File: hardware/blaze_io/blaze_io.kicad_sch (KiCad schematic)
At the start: 58 parts, among them J1 Conn_01x04, J2 Conn_01x04, J3 JTAG, J4 Conn_01x03_Pin, J5 Conn_01x03_Pin, J6 Conn_01x03_Pin, J7 Conn_01x03_Pin, J8 Conn_01x30_Pin, J9 Conn_01x30_Socket, Q1 AO4892, Q2 AO4892, SW1 SW_SPST, SW2 SW_SPDT, U1 4081, U2 TCAN1044VDDFR, U3 STM32H503KBUx

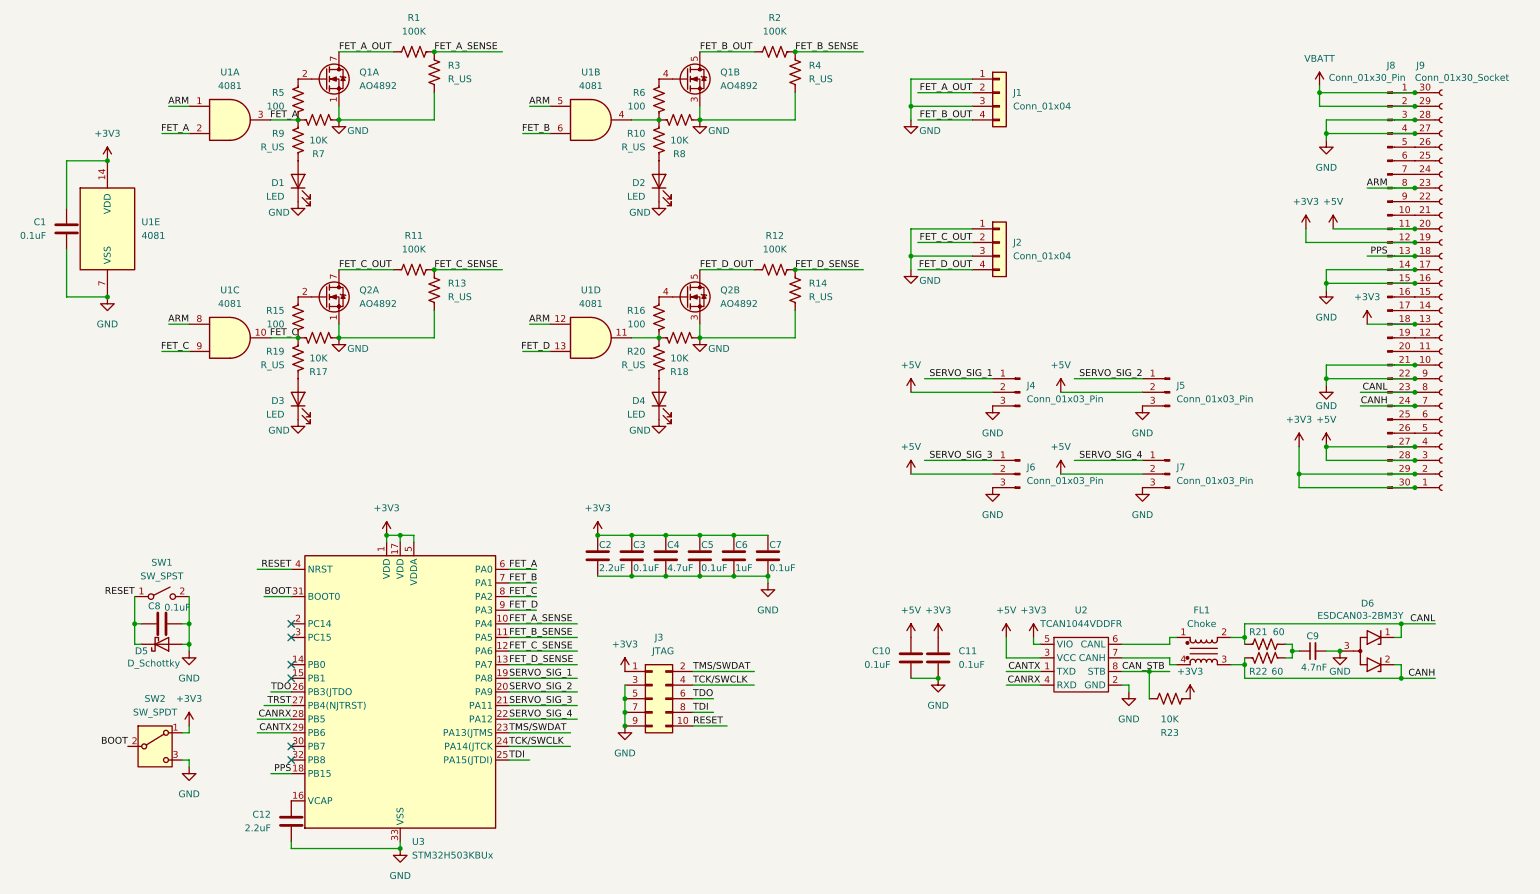
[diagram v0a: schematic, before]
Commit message: Component grouping
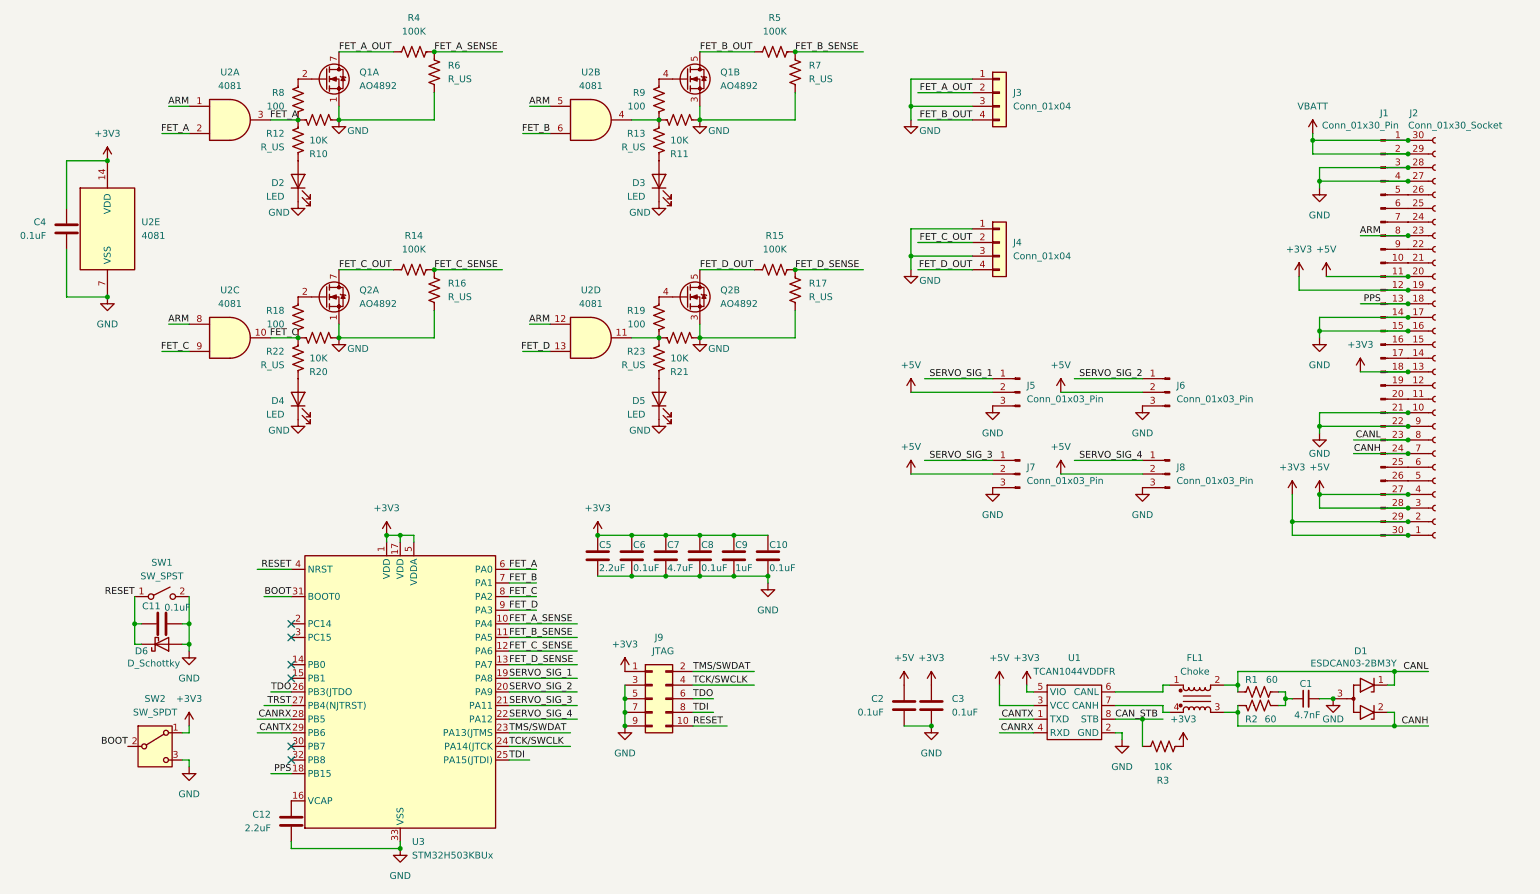
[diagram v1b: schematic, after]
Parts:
- J3: renamed from J1; footprint (none) -> TerminalBlock_TE-Connectivity:TerminalBlock_TE_282834-4_1x04_P2.54mm_Horizontal
- J4: renamed from J2; footprint (none) -> TerminalBlock_TE-Connectivity:TerminalBlock_TE_282834-4_1x04_P2.54mm_Horizontal
- J5: renamed from J4; footprint (none) -> Connector_PinHeader_2.54mm:PinHeader_1x03_P2.54mm_Vertical
- J6: renamed from J5; footprint (none) -> Connector_PinHeader_2.54mm:PinHeader_1x03_P2.54mm_Vertical
- J7: renamed from J6; footprint (none) -> Connector_PinHeader_2.54mm:PinHeader_1x03_P2.54mm_Vertical
- J8: renamed from J7; footprint (none) -> Connector_PinHeader_2.54mm:PinHeader_1x03_P2.54mm_Vertical
- J9: renamed from J3; footprint Connector_PinHeader_1.00mm:PinHeader_2x05_P1.00mm_Vertical_SMD -> Connector_PinHeader_2.54mm:PinHeader_2x05_P2.54mm_Vertical
- U2: renamed from U1; footprint (none) -> Package_SO:SOIC-14_3.9x8.7mm_P1.27mm
- renumbered C9 to C1, C7 to C10, C8 to C11, C10 to C2, C11 to C3, C1 to C4, C2 to C5, C3 to C6, C4 to C7, C5 to C8, C6 to C9, D6 to D1, D1 to D2, D2 to D3, D3 to D4, D4 to D5, D5 to D6, J8 to J1, J9 to J2, R21 to R1, R7 to R10, R8 to R11, R9 to R12, R10 to R13, R11 to R14, R12 to R15, R13 to R16, R14 to R17, R15 to R18, R16 to R19, R22 to R2, R17 to R20, R18 to R21, R19 to R22, R20 to R23, R23 to R3, R1 to R4, R2 to R5, R3 to R6, R4 to R7, R5 to R8, R6 to R9, U2 to U1
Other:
- moved on the sheet: C1, C2, C3, D1, FL1, J1, J2, R1, R2, R3, U1

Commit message: PCB Work
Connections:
- net +5V: now also J1.25 (Pin_25), J1.26 (Pin_26), J2.5 (Pin_5), J2.6 (Pin_6)
- net FET_A: now also U3.8 (PA2); no longer R10.1, R12.1, R8.2, U2.3, U3.6 (PA0)
- net FET_A_SENSE: now also U3.13 (PA7); no longer U3.10 (PA4)
- net FET_B: now also U3.9 (PA3); no longer U3.7 (PA1)
- net FET_B_SENSE: now also U3.12 (PA6); no longer U3.11 (PA5)
- net FET_C: now also U3.6 (PA0); no longer R18.2, R20.1, R22.1, U2.10, U3.8 (PA2)
- net FET_C_SENSE: now also U3.11 (PA5); no longer U3.12 (PA6)
- net FET_D: now also U3.7 (PA1); no longer U3.9 (PA3)
- net FET_D_SENSE: now also U3.10 (PA4); no longer U3.13 (PA7)
- net GND: no longer J3.1 (Pin_1), J3.3 (Pin_3), J4.1 (Pin_1), J4.3 (Pin_3)
- net VBATT: now also J3.1 (Pin_1), J3.3 (Pin_3), J4.1 (Pin_1), J4.3 (Pin_3)
- new net: R10.1, R12.1, R8.2, U2.3
- new net: R18.2, R20.1, R22.1, U2.10
